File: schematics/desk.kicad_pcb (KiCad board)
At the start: 2 copper layers, 194 x 110 mm, 36 parts, among them K1 energized = UP (raises desk), K2 energized = DOWN (lowers desk), Q1 IRLZ44N, Q2 2N7000, Q3 2N7000, Q4 BC337, Q5 BC327, U1 LM2596HV 29V-5V, U3 74HC123 250ms, U5 ACS724xLCTR-05AB, U6 74HC08

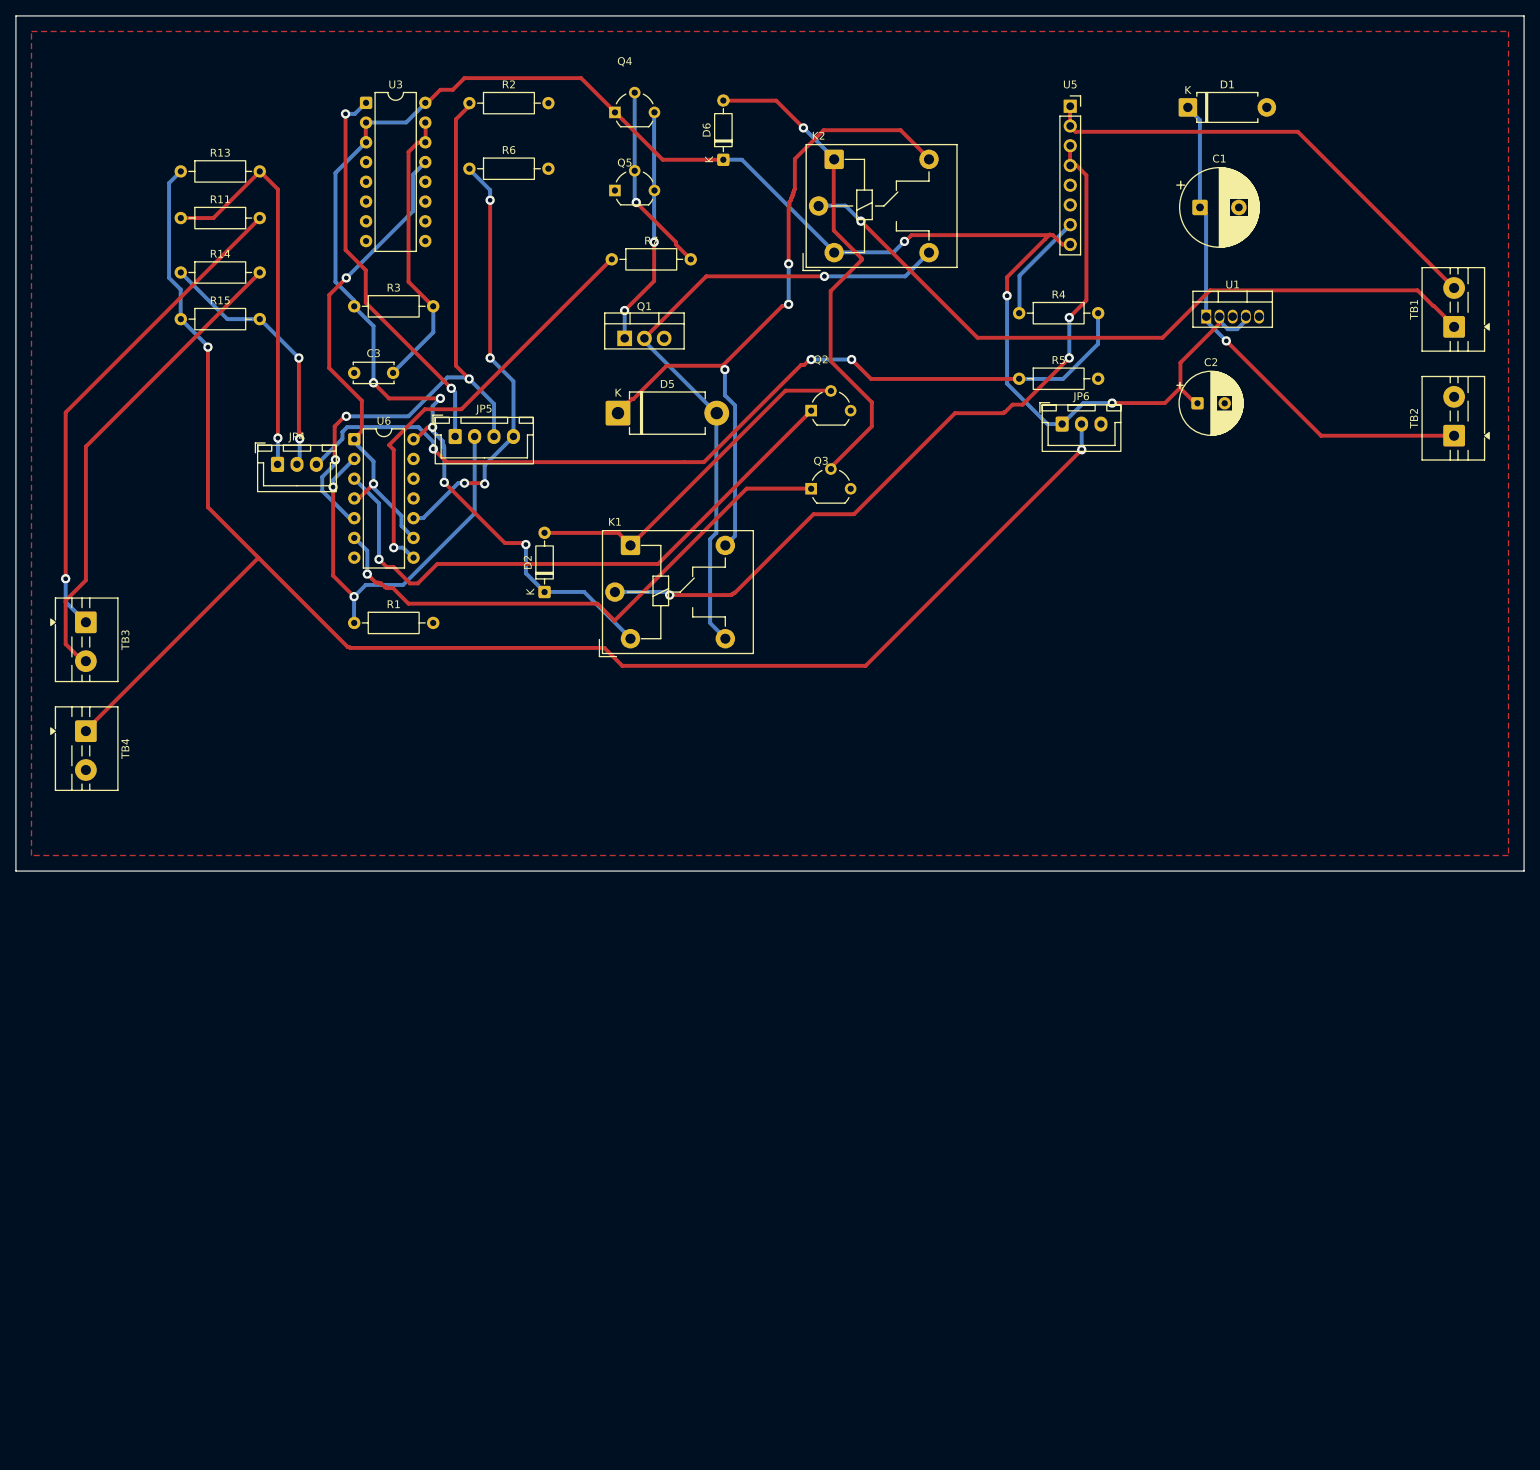
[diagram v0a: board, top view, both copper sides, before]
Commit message: Reduce via count 46 -> 33 with placement optimization before routing
Ran KiCadRoutingTools' place_optimize.py (greedy quench: nudges, 90-degree
rotations, same-footprint swaps) on the unrouted placement before routing,
locking connectors/terminal blocks (JP*/TB*) in place and ignoring GND
(zone-poured, not a real airwire concern). Airwire crossings dropped
96 -> 38, length 1763mm -> 1521mm; re-routing that placement (same
settings as before: F.Cu+B.Cu, 0.5mm track, 0.4mm clearance) completed
27/27 nets and 74/74 pads with 33 vias instead of 46 - fewer hand-soldered
wire-throughs if self-milled, same DRC-clean result (0 electrical
violations; 3 cosmetic silkscreen-text-overlap warnings from parts sitting
closer together, not fixed here).
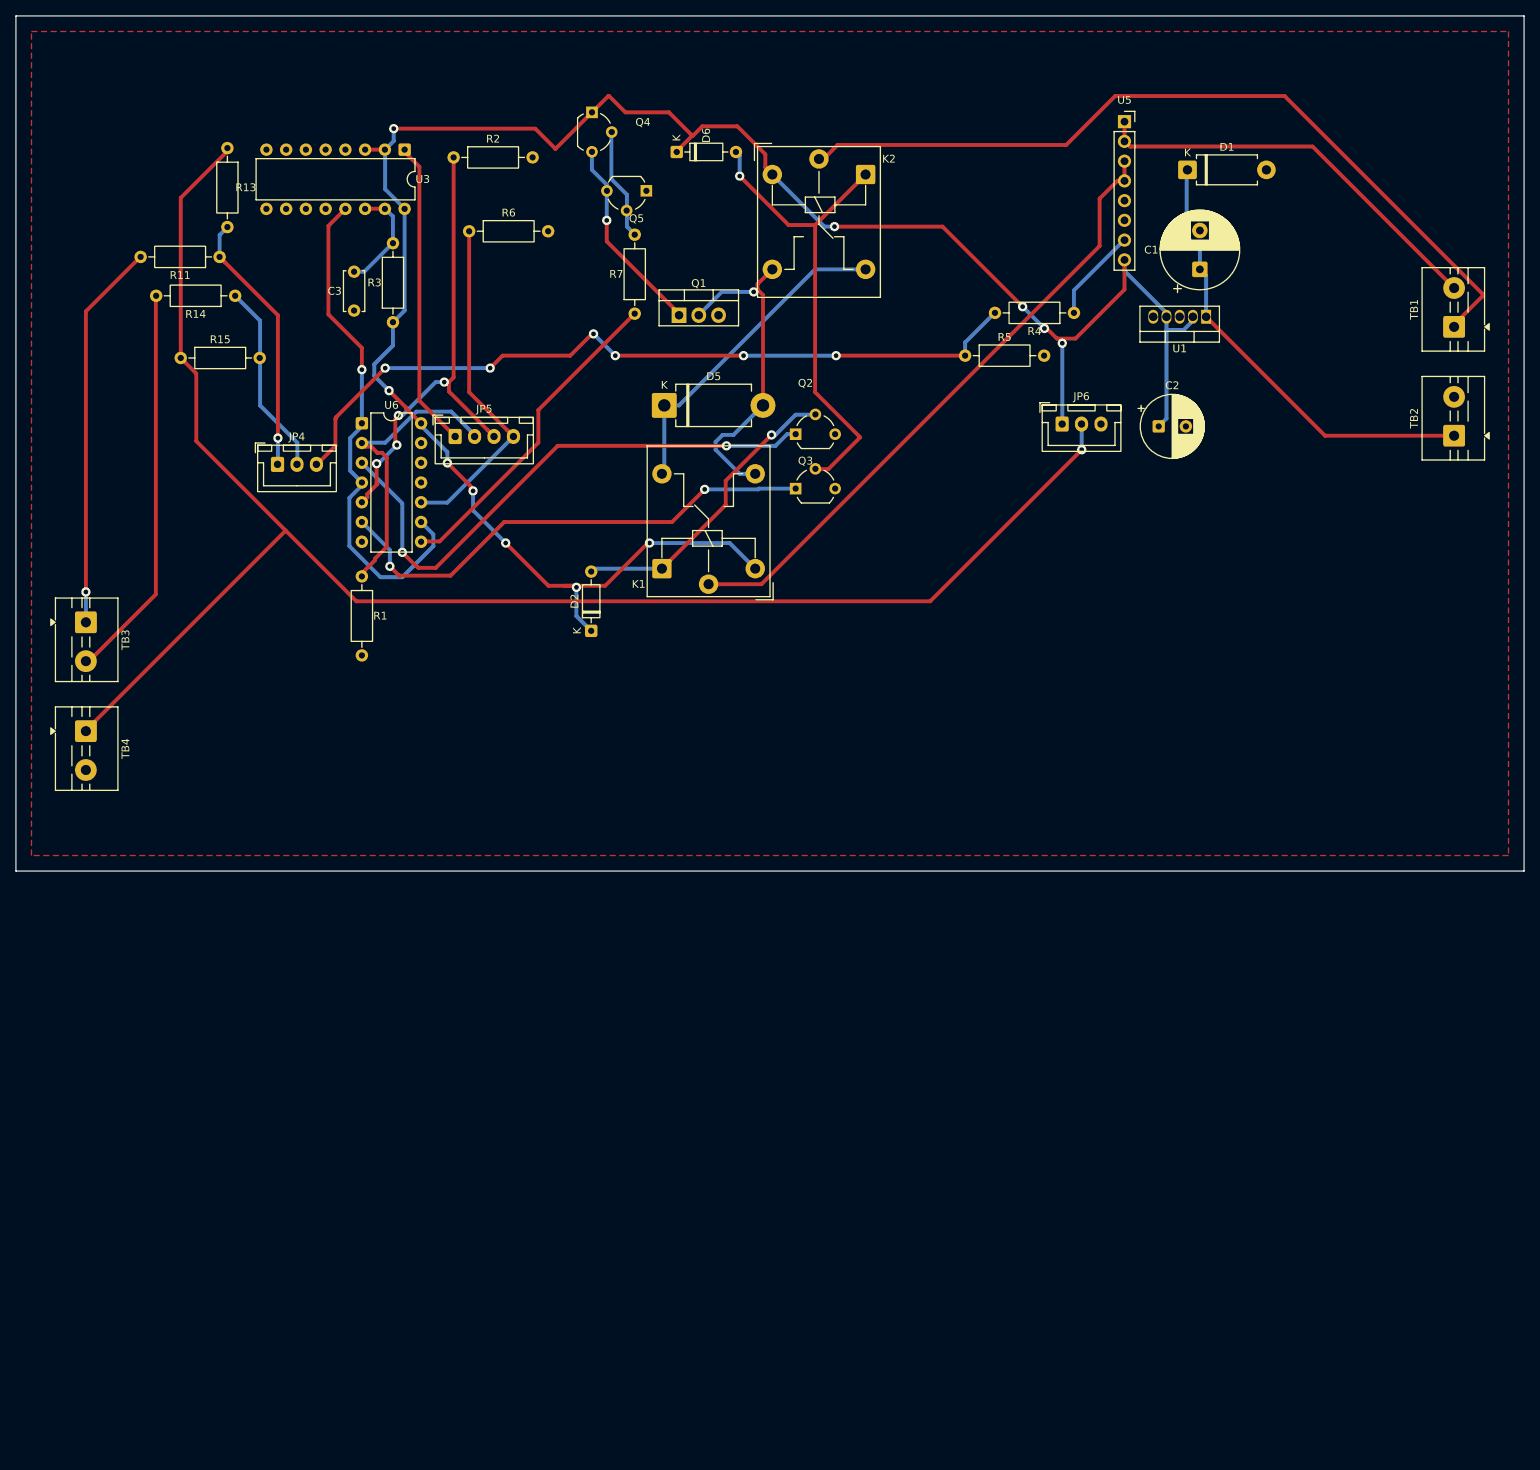
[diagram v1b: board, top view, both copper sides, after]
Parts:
- moved R6 8.05 mm to (58.3, 27.7)
- moved D1 8.03 mm to (150.7, 19.8)
- moved C3 8.02 mm to (43.5, 37.9), turned to 90 degrees
- moved C1 7.97 mm to (152.3, 32.6), turned to 90 degrees
- moved D2 7.80 mm to (74.0, 79.1)
- moved U3 7.80 mm to (50.0, 17.2), turned to -90 degrees
- moved R14 7.61 mm to (28.2, 36.0), turned to 180 degrees
- moved Q1 7.60 mm to (85.3, 38.5)
- moved R7 7.59 mm to (79.6, 38.3), turned to 90 degrees
- moved R5 7.56 mm to (122.1, 43.7)
- moved R2 7.27 mm to (56.3, 18.2)
- moved U5 7.25 mm to (142.6, 13.6)
- moved R11 7.07 mm to (26.2, 31.0), turned to 180 degrees
- moved R4 7.05 mm to (136.1, 38.2), turned to 180 degrees
- moved R13 6.70 mm to (27.2, 17.0), turned to -90 degrees
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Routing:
- net VSW: track 91.0 -> 41.6 mm, vias 3 -> 0
- net /MRET: track 84.4 -> 42.3 mm
- net Net-(U3A-Cext): track 37.2 -> 13.9 mm
- net DIR_B: track 78.8 -> 59.0 mm, vias 3 -> 4
- net /DRV_UP: track 100.6 -> 81.1 mm, vias 3 -> 0
- net ISENSE: track 117.2 -> 100.1 mm, vias 3 -> 6
- net SW_UP: track 50.9 -> 34.0 mm
- net DIR_A: track 53.2 -> 37.6 mm, vias 2 -> 0
- net Net-(TB3-Pin_1): track 63.4 -> 49.9 mm
- net Net-(R7-Pad1): track 55.0 -> 42.1 mm, vias 1 -> 0
- net PWM: track 55.5 -> 44.2 mm, vias 4 -> 0
- net Net-(TB1-Pin_1): track 93.2 -> 104.4 mm, vias 1 -> 0
- net KICK: track 50.5 -> 39.3 mm, vias 2 -> 0
- net Net-(TB3-Pin_2): track 61.3 -> 50.6 mm
- net Net-(Q4-B): track 24.1 -> 14.4 mm, vias 1 -> 0
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
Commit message: Re-route with Freerouting: 33 vias -> 1 via, still fully DRC-clean
KiCadRoutingTools' placement-quench experiments (8mm/20mm displacement,
plus the DIR_A/DIR_B gate swap) got via count down from 46 to 22 through
successive placement improvements. Trying Freerouting (mature, JAR-based,
via the classic Specctra DSN/SES workflow) on the ORIGINAL, un-optimized
placement instead - no quench needed at all - produced a 1-via, 0-DRC-
violation result outright. Its rip-up-and-reroute optimizer just handles
via minimization far better than the grid-based A* approach.

Gotchas hit along the way, for future reference:
- pcbnew.ExportSpecctraDSN() does not carry over the board's real netclass
  (track width/clearance/via size) - it always writes generic small
  defaults (0.2mm/0.2mm/0.6mm-0.3mm via). Had to text-patch the exported
  .dsn's rule and via-padstack sections to the real spec (0.5mm/0.4mm/
  1.2mm-0.6mm via) before routing, or it happily produces a board that
  doesn't meet this project's actual constraints.
- The freerouting JAR needs `-Djava.awt.headless=true`: this shell's
  inherited VSCode-snap GTK env vars (GTK_PATH etc pointing at
  /snap/code/.../gtk-3.0) otherwise crash the JVM with a glibc/pthread
  symbol-lookup error trying to initialize AWT's GTK look-and-feel, even
  though the batch CLI mode never needs a GUI at all.

1 via is trivial to hand-solder-through even on a self-milled board -
meaningfully changes the risk picture from the 16-jumper single-layer
result that started this whole investigation (see main branch's
WIRING.md / README §5 item 10).
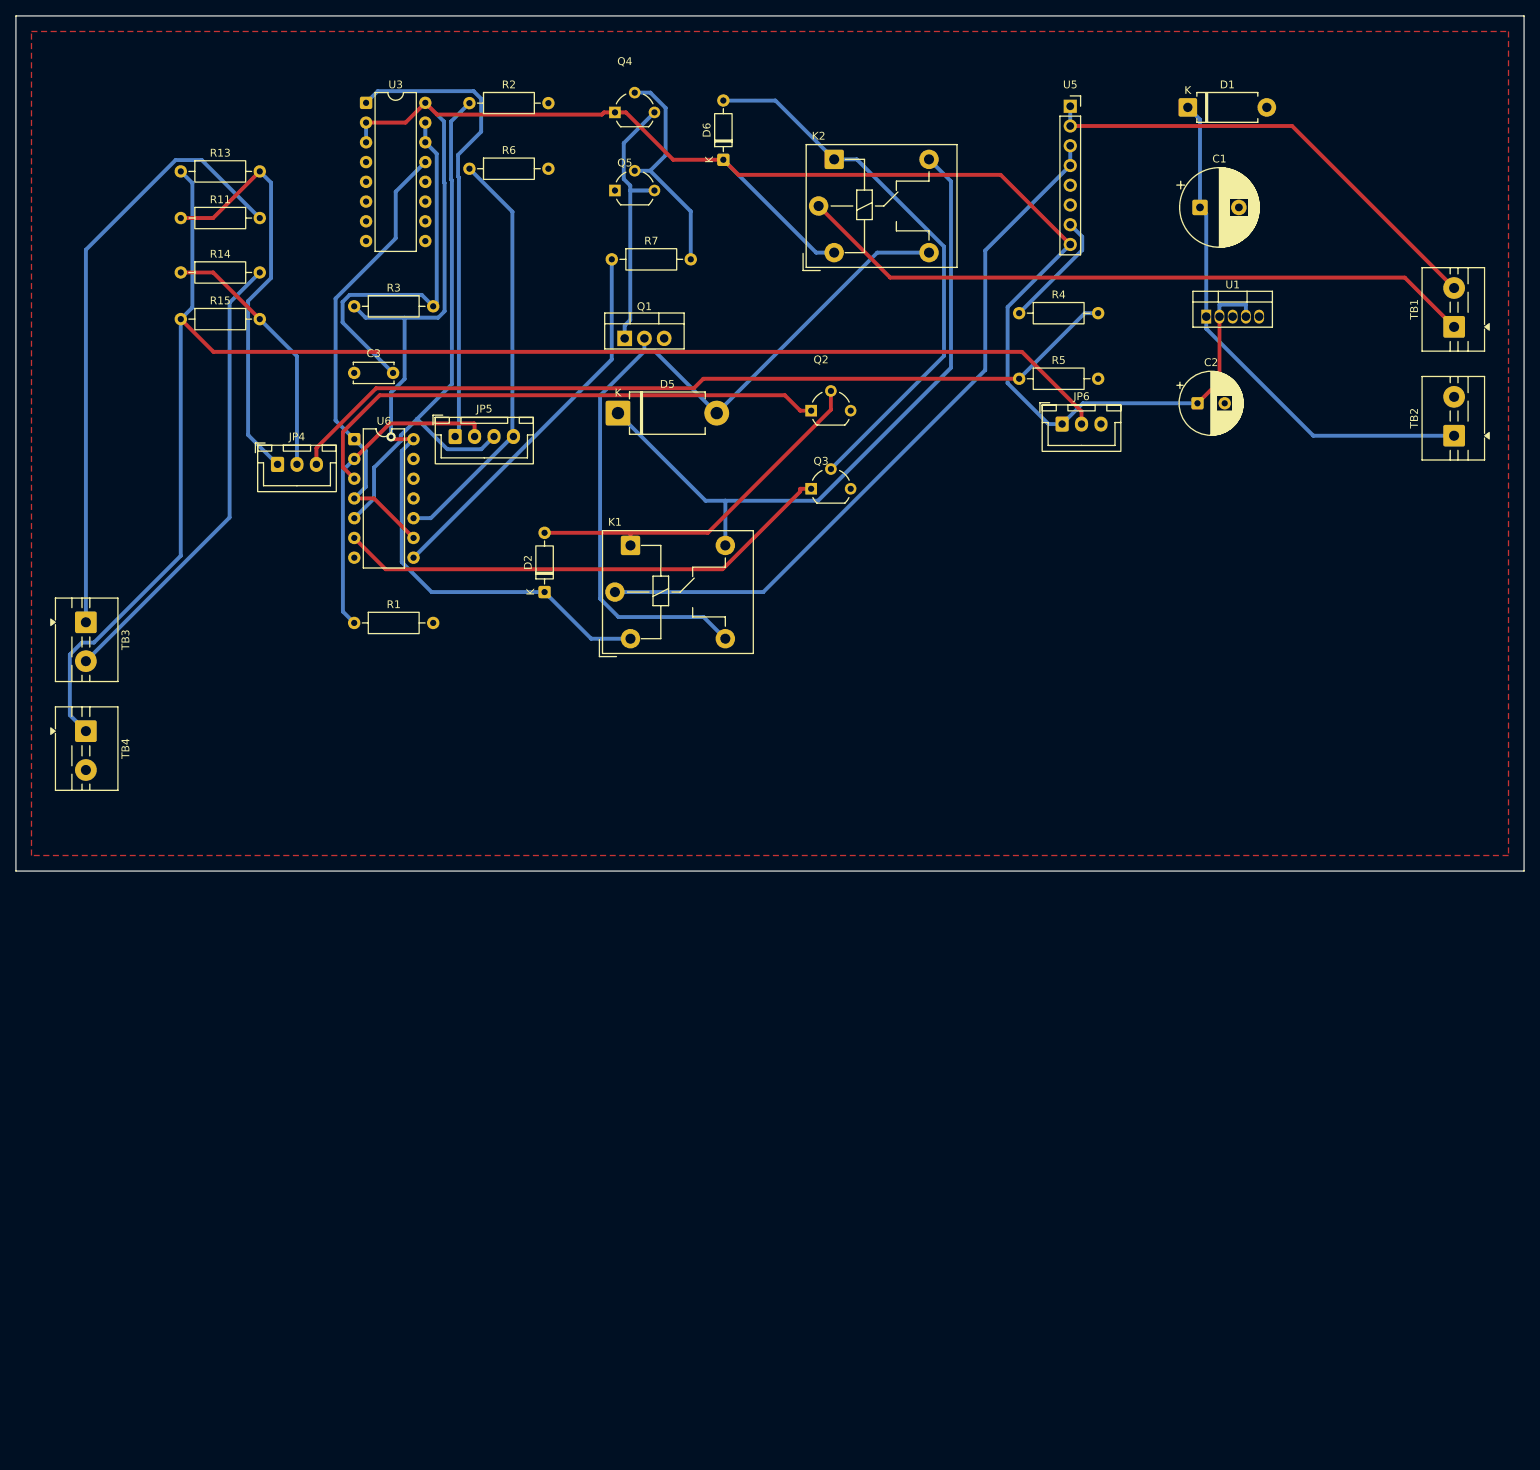
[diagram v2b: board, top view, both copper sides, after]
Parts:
- moved R6 8.05 mm to (58.3, 19.7)
- moved D1 8.03 mm to (150.7, 11.8)
- moved C3 8.02 mm to (43.5, 45.9), turned to 0 degrees
- moved C1 7.97 mm to (152.3, 24.6), turned to 0 degrees
- moved D2 7.80 mm to (68.0, 74.1)
- moved U3 7.80 mm to (45.0, 11.2), turned to 0 degrees
- moved R14 7.61 mm to (21.2, 33.0), turned to 0 degrees
- moved Q1 7.60 mm to (78.3, 41.5)
- moved R7 7.59 mm to (76.6, 31.3), turned to 0 degrees
- moved R5 7.56 mm to (129.1, 46.7)
- moved R2 7.27 mm to (58.3, 11.2)
- moved U5 7.25 mm to (135.6, 11.6)
- moved R11 7.07 mm to (21.2, 26.0), turned to 0 degrees
- moved R4 7.05 mm to (129.1, 38.2), turned to 0 degrees
- moved R13 6.70 mm to (21.2, 20.0), turned to 0 degrees
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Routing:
- net /MRET: track 42.3 -> 102.5 mm, vias 1 -> 0
- net VSW: track 41.6 -> 88.3 mm
- net Net-(U3A-Cext): track 13.9 -> 48.9 mm
- net Net-(TB3-Pin_1): track 49.9 -> 78.2 mm, vias 1 -> 0
- net +5V: track 271.6 -> 298.3 mm, vias 11 -> 1
- net KICK: track 39.3 -> 60.8 mm
- net SW_UP: track 34.0 -> 53.7 mm, vias 1 -> 0
- net Net-(TB1-Pin_1): track 104.4 -> 88.2 mm
- net Net-(Q4-B): track 14.4 -> 29.2 mm
- net DIR_B: track 59.0 -> 71.8 mm, vias 4 -> 0
- net /DRV_UP: track 81.1 -> 92.9 mm
- net PWM: track 44.2 -> 53.9 mm
- net ISENSE: track 100.1 -> 109.8 mm, vias 6 -> 0
- net Net-(TB2-Pin_1): track 57.8 -> 67.0 mm
- net Net-(D6-A): track 61.6 -> 70.8 mm, vias 1 -> 0
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
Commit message: Long shot: bring U2 back on-board - works, once its footprint is fixed
Removed the off-board ESP32 pigtail arrangement (JP1/JP2/JP3, and the
JP4/JP5/JP6 on-board mates - kept in the schematic as on_board=False
since their own wiring still anchors TB3/TB4/R11/R13/R14/R15's layout)
and placed U2 directly on the board instead, wired straight to U3/U6/
the rocker dividers/R4-R5 by matching label, the same mechanism WDOG
already uses. Board expanded to 194x150mm to fit U2's real footprint.

First attempt used the existing MCU.footprint - a generic 2x22 header
with both rows only 2.54mm apart - and Freerouting got stuck at 9/68
nets unrouted after 10 passes and 100+GB allocated, a real regression
from the off-board board's clean 1-via result. Turned out to be the
footprint, not U2's presence: that symbol's own comment already flagged
it as "a generic dual-row placeholder" needing the real DevKitC's row
spacing - which is 1 inch (25.4mm), not 2.54mm (confirmed against a
real board's dimension drawing). A 2.54mm-spaced 44-pin footprint is a
solid wall to a router; a real connector has a channel down the middle.

Built the correct footprint (two PinSocket_1x22_P2.54mm's, 25.4mm
apart - local.pretty/, wired up via fp-lib-table) and re-routed: 9
seconds, 0/68 unrouted, 3 vias, DRC clean except one pre-existing-style
GND-to-pour-zone gap on D1 (same minor category seen on other branches,
not a routing failure). Comparable to the off-board result (1 via) and
nothing like the stuck 9-unrouted state the wrong footprint produced.

Conclusion: U2 CAN come back on-board without real cost, given a
correctly-dimensioned footprint - the earlier "doesn't work" finding
was an artifact of bad footprint data, not board density. Pin-to-side
numbering (1-22/23-44) is still a placeholder pending the real board's
own silkscreen/datasheet.
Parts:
- removed JP4: JST_XH_B3B-XH-A_1x03_P2.50mm_Vertical, JST_XH_B3B-XH-A_1x03_P2.50mm_Vertical
- removed JP5: drive pigtail, JST_XH_B4B-XH-A_1x04_P2.50mm_Vertical
- removed JP6: power pigtail, JST_XH_B3B-XH-A_1x03_P2.50mm_Vertical
- added U2: PinSocket_1x22_P2.54mm_Vertical, local:DevKitC_2x22_P2.54mm_1in_row, F.Cu at (85.0, 120.0)
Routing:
- net DIR_B: track 71.8 -> 202.4 mm, vias 0 -> 1
- net PWM: track 53.9 -> 182.8 mm
- net SW_DN: track 33.3 -> 154.0 mm
- net SW_UP: track 53.7 -> 170.4 mm
- net GND: track 0.00 -> 95.6 mm, vias 0 -> 2
- net DIR_A: track 41.3 -> 126.3 mm
- net KICK: track 60.8 -> 138.2 mm
- net +3V3: track 203.3 -> 171.0 mm
- net ISENSE: track 109.8 -> 137.9 mm
- net +5V: track 298.3 -> 321.3 mm, vias 1 -> 0
- net Net-(Q3-G): track 64.9 -> 87.5 mm
- net Net-(TB1-Pin_1): track 88.2 -> 106.6 mm
- net Net-(TB3-Pin_1): track 78.2 -> 61.3 mm
- net /MRET: track 102.5 -> 86.5 mm
- net Net-(U3A-Cext): track 48.9 -> 35.1 mm
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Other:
- board size 194 x 110 mm -> 194 x 185 mm
